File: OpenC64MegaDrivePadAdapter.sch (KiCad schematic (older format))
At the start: 17 parts, among them J1 CONN_01X02, J10 DB9_F_TO_C64, J2 CONN_02X03, J20 DB9_M_TO_PAD, J3 CONN_02X03, J4 CONN_C64_AMI, J99 OSHW_LOGO, Q1 BC547

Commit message: V4 schematics
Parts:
- removed J1: CONN_01X02, Pin_Headers:Pin_Header_Straight_1x02_Pitch2.54mm, symbol CONN_01X02
- removed J2, J3: CONN_02X03, Pin_Headers:Pin_Header_Straight_2x03_Pitch2.54mm, symbol CONN_02X03
- removed J4: CONN_C64_AMI, Pin_Headers:Pin_Header_Straight_1x03_Pitch2.54mm, symbol CONN_01X03
- removed J99: OSHW_LOGO, w_logo:Logo_copper_OSHW_6x6mm, symbol CONN_01X01
- removed R1: 100, Resistors_THT:R_Axial_DIN0204_L3.6mm_D1.6mm_P7.62mm_Horizontal, symbol R
- added D6: 1N4148, Diodes_THT:D_DO-35_SOD27_P7.62mm_Horizontal, symbol rescue:D
- added S1, S2, S3: JS202011CQN, Buttons_Switches_THT:SW_CuK_JS202011CQN_DPDT_Straight, symbol js202011cqn:JS202011CQN
- D1, D2, D3, D4, D5: symbol D -> rescue:D
- J10: footprint w_conn_d-sub:DB_9F -> db9:DB_9F; symbol DB9_FEMALE -> rescue:DB9_FEMALE
- J20: symbol DB9_MALE -> rescue:DB9_MALE
- Q1: symbol BC547 -> rescue:BC547
- R2: symbol R -> rescue:R
- R3: value 100k -> 10k; symbol R -> rescue:R
- R4: value 2.2k -> 100k; symbol R -> rescue:R
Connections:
- net labels added: GND
- net labels removed: +5v, gnd
- wire segments 63 -> 67
- no-connect marks 2 -> 1

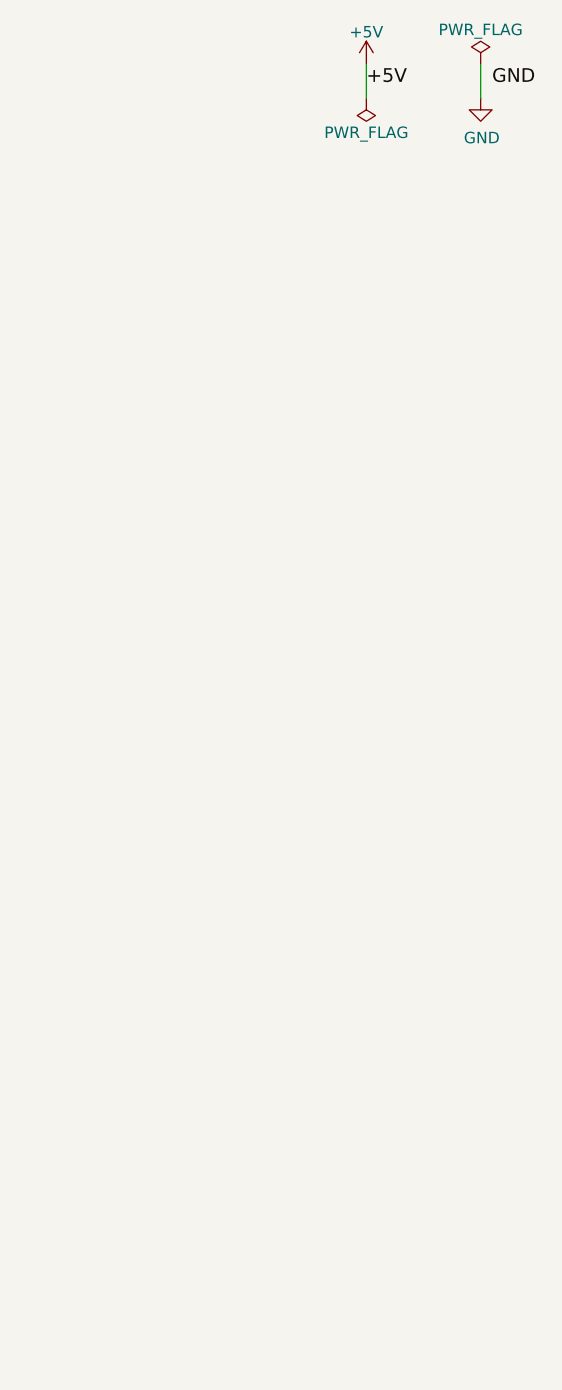
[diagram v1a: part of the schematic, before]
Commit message: Added voids elements for the silk screen
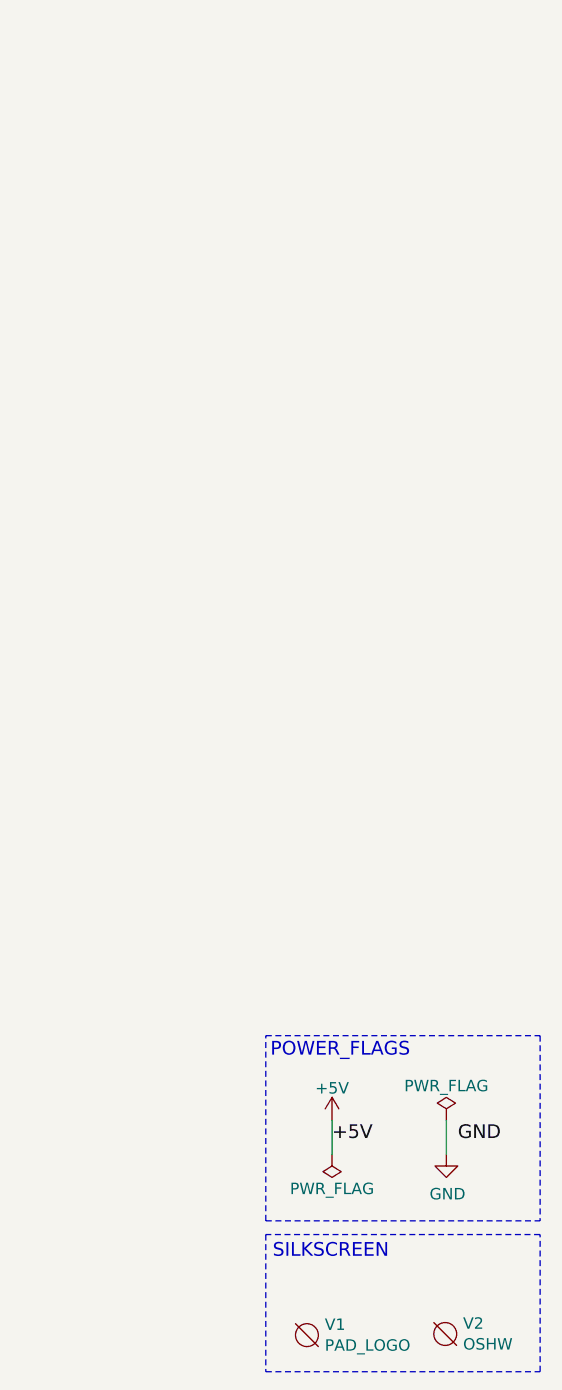
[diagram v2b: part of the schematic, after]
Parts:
- added V1: PAD_LOGO, OpenC64MegaDrivePadAdapter:LOGO, symbol void:Void
- added V2: OSHW, OpenC64MegaDrivePadAdapter:oshw, symbol void:Void
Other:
- note added: "POWER_FLAGS"
- note added: "SILKSCREEN"
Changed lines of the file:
@@
 EESchema Schematic File Version 4
+LIBS:OpenC64MegaDrivePadAdapter-cache
 EELAYER 26 0
 EELAYER END
@@
 L power:+5V #PWR02
 U 1 1 59C8A8B9
-P 10400 750
-F 0 "#PWR02" H 10400 600 50  0001 C CNN
-F 1 "+5V" H 10400 890 50  0000 C CNN
-F 2 "" H 10400 750 50  0001 C CNN
-F 3 "" H 10400 750 50  0001 C CNN
-	1    10400 750
+P 10250 5370
+F 0 "#PWR02" H 10250 5220 50  0001 C CNN
+F 1 "+5V" H 10250 5510 50  0000 C CNN
+F 2 "" H 10250 5370 50  0001 C CNN
+F 3 "" H 10250 5370 50  0001 C CNN
+	1    10250 5370
 	1    0    0    -1
 $EndComp
@@
 L power:PWR_FLAG #FLG03
 U 1 1 59C8A939
-P 10400 900
-F 0 "#FLG03" H 10400 975 50  0001 C CNN
-F 1 "PWR_FLAG" H 10400 1050 50  0000 C CNN
-F 2 "" H 10400 900 50  0001 C CNN
-F 3 "" H 10400 900 50  0001 C CNN
-	1    10400 900
-	-1   0    0    1
-$EndComp
-Text Label 10400 850  0    60   ~ 0
+P 10250 5520
+F 0 "#FLG03" H 10250 5595 50  0001 C CNN
+F 1 "PWR_FLAG" H 10250 5670 50  0000 C CNN
+F 2 "" H 10250 5520 50  0001 C CNN
+F 3 "" H 10250 5520 50  0001 C CNN
+	1    10250 5520
+	-1   0    0    1
+$EndComp
+Text Label 10250 5470 0    60   ~ 0
 +5V
 $Comp
 L power:PWR_FLAG #FLG04
 U 1 1 59C8A9AC
-P 10900 750
-F 0 "#FLG04" H 10900 825 50  0001 C CNN
-F 1 "PWR_FLAG" H 10900 900 50  0000 C CNN
-F 2 "" H 10900 750 50  0001 C CNN
-F 3 "" H 10900 750 50  0001 C CNN
-	1    10900 750
-	1    0    0    -1
-$EndComp
-Text Label 10950 850  0    60   ~ 0
+P 10750 5370
+F 0 "#FLG04" H 10750 5445 50  0001 C CNN
+F 1 "PWR_FLAG" H 10750 5520 50  0000 C CNN
+F 2 "" H 10750 5370 50  0001 C CNN
+F 3 "" H 10750 5370 50  0001 C CNN
+	1    10750 5370
+	1    0    0    -1
+$EndComp
+Text Label 10800 5470 0    60   ~ 0
 GND
 $Comp
@@
 	5000 4050 7700 4050
 Wire Wire Line
-	10400 750  10400 900
-Wire Wire Line
-	10900 750  10900 900
+	10250 5370 10250 5520
+Wire Wire Line
+	10750 5370 10750 5520
 Wire Wire Line
 	4700 2100 5000 2100
@@
 L power:GND #PWR0101
 U 1 1 5C264AB3
-P 10900 900
-F 0 "#PWR0101" H 10900 650 50  0001 C CNN
-F 1 "GND" H 10905 727 50  0000 C CNN
-F 2 "" H 10900 900 50  0001 C CNN
-F 3 "" H 10900 900 50  0001 C CNN
-	1    10900 900
+P 10750 5520
+F 0 "#PWR0101" H 10750 5270 50  0001 C CNN
+F 1 "GND" H 10755 5347 50  0000 C CNN
+F 2 "" H 10750 5520 50  0001 C CNN
+F 3 "" H 10750 5520 50  0001 C CNN
+	1    10750 5520
 	1    0    0    -1
 $EndComp
@@
 Wire Wire Line
 	5000 2600 5000 3950
+$Comp
+L void:Void V1
+U 1 1 5C325267
+P 10140 6310
+F 0 "V1" H 10218 6356 50  0000 L CNN
+F 1 "PAD_LOGO" H 10218 6265 50  0000 L CNN
+F 2 "OpenC64MegaDrivePadAdapter:LOGO" H 10140 6310 50  0001 C CNN
+F 3 "" H 10140 6310 50  0001 C CNN
+	1    10140 6310
+	1    0    0    -1
+$EndComp
+$Comp
+L void:Void V2
+U 1 1 5C3253C9
+P 10745 6305
+F 0 "V2" H 10823 6351 50  0000 L CNN
+F 1 "OSHW" H 10823 6260 50  0000 L CNN
+F 2 "OpenC64MegaDrivePadAdapter:oshw" H 10745 6305 50  0001 C CNN
+F 3 "" H 10745 6305 50  0001 C CNN
+	1    10745 6305
+	1    0    0    -1
+$EndComp
+Wire Notes Line
+	9960 6470 11160 6470
+Wire Notes Line
+	11160 6470 11160 5870
+Wire Notes Line
+	11160 5870 9960 5870
+Wire Notes Line
+	9960 5870 9960 6470
+Text Notes 9990 5980 0    60   ~ 0
+SILKSCREEN
+Wire Notes Line
+	11160 5000 11160 5810
+Wire Notes Line
+	9960 5810 9960 5000
+Text Notes 9980 5100 0    60   ~ 0
+POWER_FLAGS
+Wire Notes Line
+	9960 5810 11160 5810
+Wire Notes Line
+	9960 5000 11160 5000
 $EndSCHEMATC

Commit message: rev. 5 schematics
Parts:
- removed R3: 10k, Resistors_THT:R_Axial_DIN0204_L3.6mm_D1.6mm_P7.62mm_Horizontal, symbol rescue:R
- added Q2: BC547, TO_SOT_Packages_THT:TO-92_Molded_Narrow, symbol rescue:BC547
- added R1, R2: 10k, Resistors_THT:R_Axial_DIN0204_L3.6mm_D1.6mm_P7.62mm_Horizontal, symbol rescue:R
- R3: renamed from R2; value 2.2k -> 10k
- R4: value 100k -> 10k
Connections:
- net +5V: now also R4.1, R2.1
- net GND: now also S3.1, Q2.3 (E)
- net md_b/~a: now also S1.2; no longer S1.5
- net md_c/~st: now also S1.5; no longer S1.2
- net pot_x: now also S3.5; no longer S3.2
- net at D5.1 (K): now also S2.4; no longer S2.3
- net at Q1.1 (C), R3.2, S3.3: now also S3.4
- net at Q1.2 (B): now also R1.2; no longer R4.2
- net at S1.3, S1.4: now also S2.5; no longer S2.2
- net at S2.6: now also R1.1, R2.2
- net at S3.6: now also R4.2, Q2.1 (C)
- new net: Q2.2 (B), S3.2
- now unconnected: S2.1
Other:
- note added: "POWER FLAGS"
- note removed: "POWER_FLAGS"
- moved on the sheet: D1, D2, D3, D4, D5, D6, J10, R3, S3

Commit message: rev 6
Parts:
- added R5: 10k, Resistor_THT:R_Axial_DIN0204_L3.6mm_D1.6mm_P7.62mm_Horizontal, symbol rescue:R
- D1, D2, D3, D4, D5, D6: footprint Diodes_THT:D_DO-35_SOD27_P7.62mm_Horizontal -> Diode_THT:D_DO-35_SOD27_P7.62mm_Horizontal
- J10: footprint db9:DB_9F -> OpenC64MegaDrivePadAdapter:DB_9F
- J20: footprint w_conn_d-sub:DB_9M -> OpenC64MegaDrivePadAdapter:DB_9M
- Q1, Q2: footprint TO_SOT_Packages_THT:TO-92_Molded_Narrow -> Package_TO_SOT_THT:TO-92L_HandSolder
- R1, R2, R3, R4: footprint Resistors_THT:R_Axial_DIN0204_L3.6mm_D1.6mm_P7.62mm_Horizontal -> Resistor_THT:R_Axial_DIN0204_L3.6mm_D1.6mm_P7.62mm_Horizontal
- S1, S2, S3: footprint Buttons_Switches_THT:SW_CuK_JS202011CQN_DPDT_Straight -> Button_Switch_THT:SW_CuK_JS202011CQN_DPDT_Straight
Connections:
- net +5V: now also R5.1; no longer J20.7
- net pot_y renamed md_sel
- net md_sel: now also J20.7, R5.2
- no-connect marks 1 -> 3
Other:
- moved on the sheet: D1, D2, D3, D4, D5, D6, J10, J20, Q1, Q2, R1, R2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
